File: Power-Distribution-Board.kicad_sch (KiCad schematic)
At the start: 0 parts

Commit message: Started Schematic and PCB layout
Life is pain, I hate-
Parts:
- added J1: XT60PB-F, XT60PBF, symbol XT60PB-F:XT60PB-F
- added J10, J11, J2, J3, J4, J5, J6, J7, J8, J9: XT30UPB-F, XT30UPBF, symbol XT30UPB-F:XT30UPB-F
- added J12: XT90PB-F, XT90PBF, symbol XT90PB-F:XT90PB-F
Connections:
- new net: J1.1 (+), J10.1, J11.1, J12.1, J2.1, J3.1, J4.1, J5.1, J6.1, J7.1, J8.1, J9.1
- new net: J1.2 (-), J10.2, J11.2, J12.2, J2.2, J3.2, J4.2, J5.2, J6.2, J7.2, J8.2, J9.2

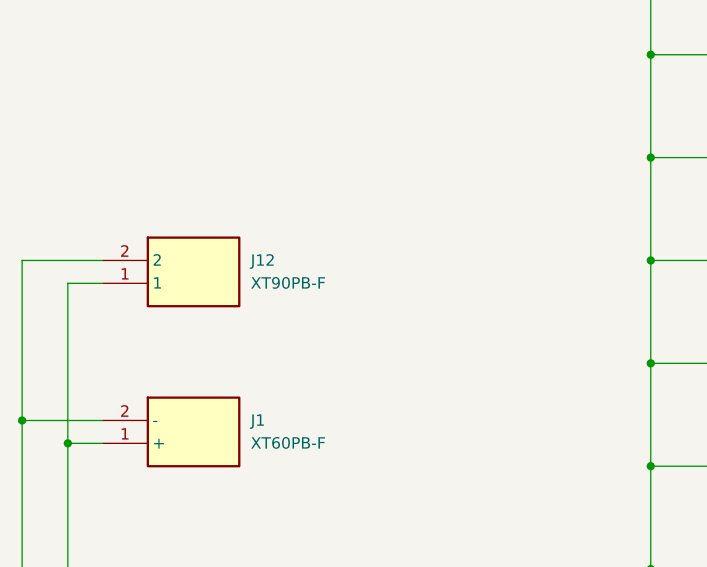
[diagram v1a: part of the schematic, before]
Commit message: XT90 fully transitioned to male
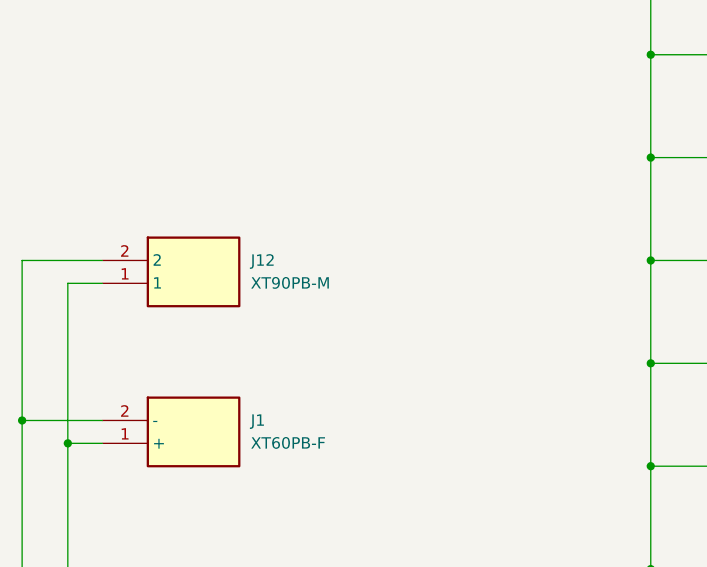
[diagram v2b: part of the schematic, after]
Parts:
- removed J12: XT90PB-F, XT90PBF, symbol XT90PB-F:XT90PB-F
- added J12: XT90PB-M, XT90PBM, symbol XT90PB-M:XT90PB-M
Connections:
- net at J1.1 (+), J10.1, J11.1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: now also J12.1
- net at J1.2 (-), J10.2, J11.2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: now also J12.2
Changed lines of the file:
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@@
+	)
+	(symbol
+		(lib_id "XT90PB-M:XT90PB-M")
+		(at 138.43 88.9 0)
+		(unit 1)
+		(exclude_from_sim no)
+		(in_bom yes)
+		(on_board yes)
+		(dnp no)
+		(fields_autoplaced yes)
+		(property "Reference" "J12"
+			(at 154.94 88.8999 0)
+			(effects
+				(font
+					(size 1.27 1.27)
+				)
+				(justify left)
+			)
+		)
+		(property "Value" "XT90PB-M"
+			(at 154.94 91.4399 0)
+			(effects
+				(font
+					(size 1.27 1.27)
+				)
+				(justify left)
+			)
+		)
+		(property "Footprint" "XT90PBM"
+			(at 154.94 183.82 0)
+			(effects
+				(font
+					(size 1.27 1.27)
+				)
+				(justify left top)
+				(hide yes)
+			)
+		)
+		(property "Datasheet" "https://www.china-amass.com/biao/439.html"
+			(at 154.94 283.82 0)
+			(effects
+				(font
+					(size 1.27 1.27)
+				)
+				(justify left top)
+				(hide yes)
+			)
+		)
+		(property "Description" "Connector: DC supply; socket; XT90; male; PIN: 2; on PCBs; THT"
+			(at 138.43 88.9 0)
+			(effects
+				(font
+					(size 1.27 1.27)
+				)
+				(hide yes)
+			)
+		)
+		(property "Height" "19.7"
+			(at 154.94 483.82 0)
+			(effects
+				(font
+					(size 1.27 1.27)
+				)
+				(justify left top)
+				(hide yes)
+			)
+		)
+		(property "Manufacturer_Name" "Amass"
+			(at 154.94 583.82 0)
+			(effects
+				(font
+					(size 1.27 1.27)
+				)
+				(justify left top)
+				(hide yes)
+			)
+		)
+		(property "Manufacturer_Part_Number" "XT90PB-F"
+			(at 154.94 683.82 0)
+			(effects
+				(font
+					(size 1.27 1.27)
+				)
+				(justify left top)
+				(hide yes)
+			)
+		)
+		(property "Mouser Part Number" ""
+			(at 154.94 783.82 0)
+			(effects
+				(font
+					(size 1.27 1.27)
+				)
+				(justify left top)
+				(hide yes)
+			)
+		)
+		(property "Mouser Price/Stock" ""
+			(at 154.94 883.82 0)
+			(effects
+				(font
+					(size 1.27 1.27)
+				)
+				(justify left top)
+				(hide yes)
+			)
+		)
+		(property "Arrow Part Number" ""
+			(at 154.94 983.82 0)
+			(effects
+				(font
+					(size 1.27 1.27)
+				)
+				(justify left top)
+				(hide yes)
+			)
+		)
+		(property "Arrow Price/Stock" ""
+			(at 154.94 1083.82 0)
+			(effects
+				(font
+					(size 1.27 1.27)
+				)
+				(justify left top)
+				(hide yes)
+			)
+		)
+		(pin "1"
+		)
+		(pin "2"
+		)
+		(instances
+			(project ""
+				(path "/7a3180e8-37a7-4541-a088-b281e2ca63ea"
+					(reference "J12")
+					(unit 1)
+				)
+			)
+		)
 	)
 	(symbol
@@
 					(unit 1)
 				)
-			)
-		)
-	)
-	(symbol
-		(lib_id "XT90PB-F:XT90PB-F")
-		(at 138.43 88.9 0)
-		(unit 1)
-		(exclude_from_sim no)
-		(in_bom yes)
-		(on_board yes)
-		(dnp no)
-		(fields_autoplaced yes)
-		(property "Reference" "J12"
-			(at 154.94 88.8999 0)
-			(effects
-				(font
-					(size 1.27 1.27)
-				)
-				(justify left)
-			)
-		)
-		(property "Value" "XT90PB-F"
-			(at 154.94 91.4399 0)
-			(effects
-				(font
-					(size 1.27 1.27)
-				)
-				(justify left)
-			)
-		)
-		(property "Footprint" "XT90PBF"
-			(at 154.94 183.82 0)
-			(effects
-				(font
-					(size 1.27 1.27)
-				)
-				(justify left top)
-				(hide yes)
-			)
-		)
-		(property "Datasheet" "https://www.china-amass.com/biao/439.html"
-			(at 154.94 283.82 0)
-			(effects
-				(font
-					(size 1.27 1.27)
-				)
-				(justify left top)
-				(hide yes)
-			)
-		)
-		(property "Description" "Connector: DC supply; socket; XT90; female; PIN: 2; on PCBs; THT"
-			(at 138.43 88.9 0)
-			(effects
-				(font
-					(size 1.27 1.27)
-				)
-				(hide yes)
-			)
-		)
-		(property "Height" "19.7"
-			(at 154.94 483.82 0)
-			(effects
-				(font
-					(size 1.27 1.27)
-				)
-				(justify left top)
-				(hide yes)
-			)
-		)
-		(property "Manufacturer_Name" "Amass"
-			(at 154.94 583.82 0)
-			(effects
-				(font
-					(size 1.27 1.27)
-				)
-				(justify left top)
-				(hide yes)
-			)
-		)
-		(property "Manufacturer_Part_Number" "XT90PB-F"
-			(at 154.94 683.82 0)
-			(effects
-				(font
-					(size 1.27 1.27)
-				)
-				(justify left top)
-				(hide yes)
-			)
-		)
-		(property "Mouser Part Number" ""
-			(at 154.94 783.82 0)
-			(effects
-				(font
-					(size 1.27 1.27)
-				)
-				(justify left top)
-				(hide yes)
-			)
-		)
-		(property "Mouser Price/Stock" ""
-			(at 154.94 883.82 0)
-			(effects
-				(font
-					(size 1.27 1.27)
-				)
-				(justify left top)
-				(hide yes)
-			)
-		)
-		(property "Arrow Part Number" ""
-			(at 154.94 983.82 0)
-			(effects
-				(font
-					(size 1.27 1.27)
-				)
-				(justify left top)
-				(hide yes)
-			)
-		)
-		(property "Arrow Price/Stock" ""
-			(at 154.94 1083.82 0)
-			(effects
-				(font
-					(size 1.27 1.27)
-				)
-				(justify left top)
-				(hide yes)
-			)
-		)
-		(pin "1"
-		)
-		(pin "2"
-		)
-		(instances
-			(project ""
-				(path "/7a3180e8-37a7-4541-a088-b281e2ca63ea"
-					(reference "J12")
-					(unit 1)
-				)

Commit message: Actually properly finally fixed the model
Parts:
- J12: Manufacturer_Part_Number XT90PB-F -> XT90PB-M
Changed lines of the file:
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@@
 			)
 		)
-		(property "Manufacturer_Part_Number" "XT90PB-F"
+		(property "Manufacturer_Part_Number" "XT90PB-M"
 			(at 154.94 683.82 0)
 			(effects
